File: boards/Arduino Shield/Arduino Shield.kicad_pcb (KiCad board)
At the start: 2 copper layers, 11 parts, among them J1 Screw_Terminal_01x09, J10 Screw_Terminal_01x04, J2 Screw_Terminal_01x09, J3 Screw_Terminal_01x09, J4 Screw_Terminal_01x09, J5 Screw_Terminal_01x09, J6 Screw_Terminal_01x09, J7 Screw_Terminal_01x09, J8 Screw_Terminal_01x09, J9 Screw_Terminal_01x09, U1 A000062

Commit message: Updated pcb
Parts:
- added D1: LED, LED_SMD:LED_0805_2012Metric, F.Cu at (221.0, 99.1)
- added D2: LED, LED_SMD:LED_0805_2012Metric, F.Cu at (219.4, 88.9)
- added D3: LED, LED_SMD:LED_0805_2012Metric, F.Cu at (220.7, 94.0)
- added D4: LED, LED_SMD:LED_0805_2012Metric, F.Cu at (220.7, 109.2)
- added D5: LED, LED_SMD:LED_0805_2012Metric, F.Cu at (221.0, 104.1)
- added J11: Screw_Terminal_01x08, TerminalBlock_4Ucon:TerminalBlock_4Ucon_1x08_P3.50mm_Horizontal, F.Cu at (238.8, 106.2)
- added R1: 6Ω, Resistor_SMD:R_0805_2012Metric, F.Cu at (215.0, 109.2)
- added R2: 6Ω, Resistor_SMD:R_0805_2012Metric, F.Cu at (215.0, 94.0)
- added R3: 6Ω, Resistor_SMD:R_0805_2012Metric, F.Cu at (215.0, 88.9)
- added R4: 230Ω, Resistor_SMD:R_0805_2012Metric, F.Cu at (214.3, 104.1)
- added R5: 6Ω, Resistor_SMD:R_0805_2012Metric, F.Cu at (215.0, 99.1)
- J1: value Screw_Terminal_01x09 -> Screw_Terminal_01x07; footprint TerminalBlock_4Ucon:TerminalBlock_4Ucon_1x09_P3.50mm_Horizontal -> TerminalBlock_4Ucon:TerminalBlock_4Ucon_1x07_P3.50mm_Horizontal
- J10: value Screw_Terminal_01x04 -> Screw_Terminal_01x03; footprint TerminalBlock_4Ucon:TerminalBlock_4Ucon_1x04_P3.50mm_Horizontal -> TerminalBlock_4Ucon:TerminalBlock_4Ucon_1x03_P3.50mm_Horizontal
- J2, J3, J4, J5, J6, J7: value Screw_Terminal_01x09 -> Screw_Terminal_01x08; footprint TerminalBlock_4Ucon:TerminalBlock_4Ucon_1x09_P3.50mm_Horizontal -> TerminalBlock_4Ucon:TerminalBlock_4Ucon_1x08_P3.50mm_Horizontal
- J8: value Screw_Terminal_01x09 -> Screw_Terminal_01x04; footprint TerminalBlock_4Ucon:TerminalBlock_4Ucon_1x09_P3.50mm_Horizontal -> TerminalBlock_4Ucon:TerminalBlock_4Ucon_1x04_P3.50mm_Horizontal
- J9: value Screw_Terminal_01x09 -> Screw_Terminal_01x10; footprint TerminalBlock_4Ucon:TerminalBlock_4Ucon_1x09_P3.50mm_Horizontal -> TerminalBlock_4Ucon:TerminalBlock_4Ucon_1x10_P3.50mm_Horizontal
- moved J4 141.7 mm to (246.3, 75.3), turned to 90 degrees
- moved J5 111.8 mm to (154.9, 38.1), turned to 0 degrees
- moved J1 104.5 mm to (147.3, 121.9), turned to 180 degrees
- moved J3 103.5 mm to (208.3, 121.9), turned to 180 degrees
- moved J9 99.1 mm to (116.8, 38.0)
- moved J6 85.7 mm to (184.7, 38.1), turned to 0 degrees
- moved J8 73.8 mm to (228.6, 85.4), turned to -90 degrees
- moved J2 55.8 mm to (177.8, 121.9), turned to 180 degrees
- moved J10 48.0 mm to (223.5, 70.2)
- moved J7 18.3 mm to (231.2, 39.3)
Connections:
- U1 pad 0: Net-(J3-Pin_9) -> Net-(J5-Pin_8)
- U1 pad 1: Net-(J3-Pin_8) -> Net-(J5-Pin_7)
- U1 pad 10: Net-(J4-Pin_8) -> Net-(J9-Pin_8)
- U1 pad 11: Net-(J4-Pin_7) -> Net-(J9-Pin_7)
- U1 pad 12: Net-(J4-Pin_6) -> Net-(J9-Pin_6)
- U1 pad 13: Net-(J4-Pin_5) -> Net-(J9-Pin_5)
- U1 pad 14: Net-(J8-Pin_1) -> Net-(J6-Pin_1)
- U1 pad 15: Net-(J8-Pin_2) -> Net-(J6-Pin_2)
- U1 pad 16: Net-(J8-Pin_3) -> Net-(J6-Pin_3)
- U1 pad 17: Net-(J8-Pin_4) -> Net-(J6-Pin_4)
- U1 pad 18: Net-(J8-Pin_5) -> Net-(J6-Pin_5)
- U1 pad 19: Net-(J8-Pin_6) -> Net-(J6-Pin_6)
- U1 pad 2: Net-(J3-Pin_7) -> Net-(J5-Pin_6)
- U1 pad 20: Net-(J8-Pin_7) -> Net-(J6-Pin_7)
- U1 pad 21: Net-(J8-Pin_8) -> Net-(J6-Pin_8)
- U1 pad 22: Net-(J1-Pin_7) -> Net-(J4-Pin_7)
- U1 pad 23: Net-(J7-Pin_1) -> Net-(J7-Pin_2)
- U1 pad 24: Net-(J1-Pin_8) -> Net-(J4-Pin_6)
- U1 pad 25: Net-(J7-Pin_2) -> Net-(J7-Pin_3)
- U1 pad 26: Net-(J1-Pin_9) -> Net-(J4-Pin_5)
- U1 pad 27: Net-(J7-Pin_3) -> Net-(J7-Pin_4)
- U1 pad 28: Net-(J5-Pin_1) -> Net-(J4-Pin_4)
- U1 pad 29: Net-(J7-Pin_4) -> Net-(J7-Pin_5)
- U1 pad 3: Net-(J3-Pin_6) -> Net-(J5-Pin_5)
- U1 pad 30: Net-(J5-Pin_2) -> Net-(J4-Pin_3)
- U1 pad 31: Net-(J7-Pin_5) -> Net-(J7-Pin_6)
- U1 pad 32: Net-(J5-Pin_3) -> Net-(J4-Pin_2)
- U1 pad 33: Net-(J7-Pin_6) -> Net-(J7-Pin_7)
- U1 pad 34: Net-(J5-Pin_4) -> Net-(J4-Pin_1)
- U1 pad 35: Net-(J7-Pin_7) -> Net-(J7-Pin_8)
- U1 pad 36: Net-(J5-Pin_5) -> Net-(J11-Pin_8)
- U1 pad 37: Net-(J7-Pin_8) -> Net-(J10-Pin_1)
- U1 pad 38: Net-(J5-Pin_6) -> Net-(J11-Pin_7)
- U1 pad 39: Net-(J7-Pin_9) -> Net-(J10-Pin_2)
- U1 pad 3V3: Net-(J2-Pin_3) -> Net-(J1-Pin_5)
- U1 pad 4: Net-(J3-Pin_5) -> Net-(J5-Pin_4)
- U1 pad 40: Net-(J5-Pin_7) -> Net-(J11-Pin_6)
- U1 pad 41: Net-(J6-Pin_1) -> Net-(J10-Pin_3)
- U1 pad 42: Net-(J5-Pin_8) -> Net-(J11-Pin_5)
- U1 pad 43: Net-(J6-Pin_2) -> Net-(J8-Pin_1)
- U1 pad 44: Net-(J5-Pin_9) -> Net-(J11-Pin_4)
- U1 pad 45: Net-(J6-Pin_3) -> Net-(J8-Pin_2)
- U1 pad 46: Net-(J10-Pin_1) -> Net-(J11-Pin_3)
- U1 pad 47: Net-(J6-Pin_4) -> Net-(J8-Pin_3)
- U1 pad 48: Net-(J10-Pin_2) -> Net-(J11-Pin_2)
- U1 pad 49: Net-(J6-Pin_5) -> Net-(U1-D49)
- U1 pad 5: Net-(J3-Pin_4) -> Net-(J5-Pin_3)
- U1 pad 50: Net-(J10-Pin_3) -> Net-(U1-D50)
- U1 pad 51: Net-(J6-Pin_6) -> Net-(U1-D51)
- U1 pad 52: Net-(J10-Pin_4) -> Net-(U1-D52)
- U1 pad 53: Net-(J6-Pin_7) -> Net-(U1-D53)
- U1 pad 5V_1: Net-(J2-Pin_4) -> Net-(J1-Pin_4)
- U1 pad 5V_2: Net-(J1-Pin_6) -> Net-(J4-Pin_8)
- U1 pad 5V_3: Net-(J8-Pin_9) -> Net-(J7-Pin_1)
- U1 pad 6: Net-(J3-Pin_3) -> Net-(J5-Pin_2)
- U1 pad 7: Net-(J3-Pin_2) -> Net-(J5-Pin_1)
- U1 pad 8: Net-(J3-Pin_1) -> Net-(J9-Pin_10)
- U1 pad 9: Net-(J4-Pin_9) -> Net-(J9-Pin_9)
- U1 pad AD1: Net-(J2-Pin_9) -> Net-(J2-Pin_7)
- U1 pad AD10: Net-(J9-Pin_9) -> Net-(J3-Pin_6)
- U1 pad AD11: Net-(J1-Pin_1) -> Net-(J3-Pin_5)
- U1 pad AD2: Net-(J9-Pin_1) -> Net-(J2-Pin_6)
- U1 pad AD3: Net-(J9-Pin_2) -> Net-(J2-Pin_5)
- U1 pad AD4: Net-(J9-Pin_3) -> Net-(J2-Pin_4)
- U1 pad AD5: Net-(J9-Pin_4) -> Net-(J2-Pin_3)
- U1 pad AD6: Net-(J9-Pin_5) -> Net-(J2-Pin_2)
- U1 pad AD7: Net-(J9-Pin_6) -> Net-(J2-Pin_1)
- U1 pad AD8: Net-(J9-Pin_7) -> Net-(J3-Pin_8)
- U1 pad AD9: Net-(J9-Pin_8) -> Net-(J3-Pin_7)
- U1 pad AREF: Net-(J4-Pin_3) -> Net-(J9-Pin_3)
- U1 pad CANRX0: Net-(J1-Pin_4) -> Net-(J3-Pin_2)
- U1 pad CANTX0: Net-(J1-Pin_5) -> Net-(J3-Pin_1)
- U1 pad DAC0: Net-(J1-Pin_2) -> Net-(J3-Pin_4)
- U1 pad DAC1: Net-(J1-Pin_3) -> Net-(J3-Pin_3)
- U1 pad GND1: Net-(J2-Pin_5) -> Net-(J1-Pin_3)
- U1 pad GND2: Net-(J2-Pin_6) -> Net-(J1-Pin_2)
- U1 pad GND3: Net-(J4-Pin_4) -> Net-(J9-Pin_4)
- U1 pad GND4: Net-(J6-Pin_9) -> Net-(J11-Pin_1)
- U1 pad GND5: Net-(J6-Pin_8) -> Net-(J8-Pin_4)
- U1 pad IOREF: Net-(J2-Pin_1) -> Net-(J1-Pin_7)
- U1 pad RESET: Net-(J2-Pin_2) -> Net-(J1-Pin_6)
- U1 pad SCL: Net-(J4-Pin_1) -> Net-(J9-Pin_1)
- U1 pad SDA: Net-(J4-Pin_2) -> Net-(J9-Pin_2)
- U1 pad VIN: Net-(J2-Pin_7) -> Net-(J1-Pin_1)

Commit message: updated pcb
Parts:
- moved J4 99.8 mm to (147.3, 88.3)
- moved J11 80.8 mm to (160.0, 88.0)
- moved D1 42.3 mm to (185.4, 76.2)
- moved D3 42.3 mm to (185.2, 71.1)
- moved D4 42.3 mm to (185.2, 86.4)
- moved D5 42.3 mm to (185.4, 81.3)
- moved D2 40.2 mm to (186.4, 66.0)
- moved R1 32.3 mm to (192.1, 86.4)
- moved R2 32.3 mm to (192.1, 71.1)
- moved R3 32.3 mm to (192.1, 66.0)
- moved R5 32.3 mm to (192.1, 76.2)
- moved R4 31.8 mm to (192.1, 81.3)
- moved J7 20.0 mm to (213.4, 48.3)
- moved J8 16.4 mm to (213.4, 91.4)
- moved J3 14.5 mm to (201.3, 109.2)
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
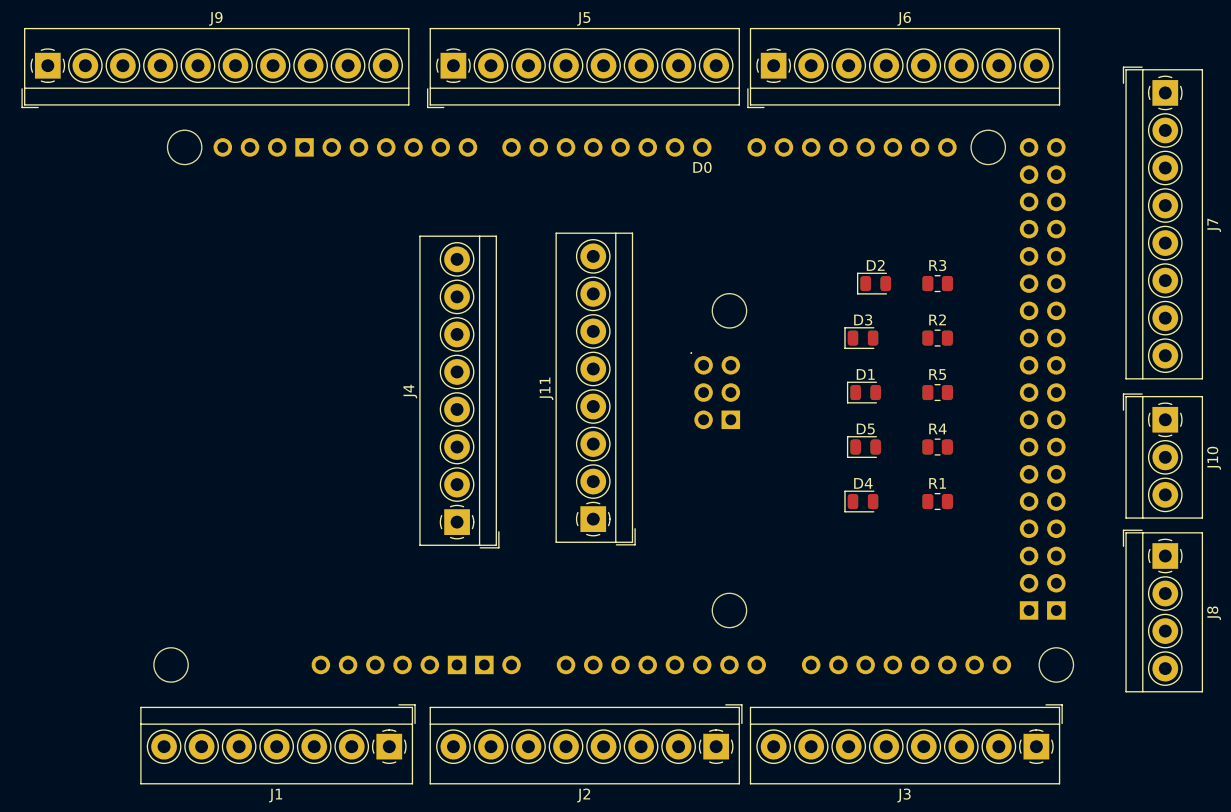
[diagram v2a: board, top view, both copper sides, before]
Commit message: Updated PCB with wiring
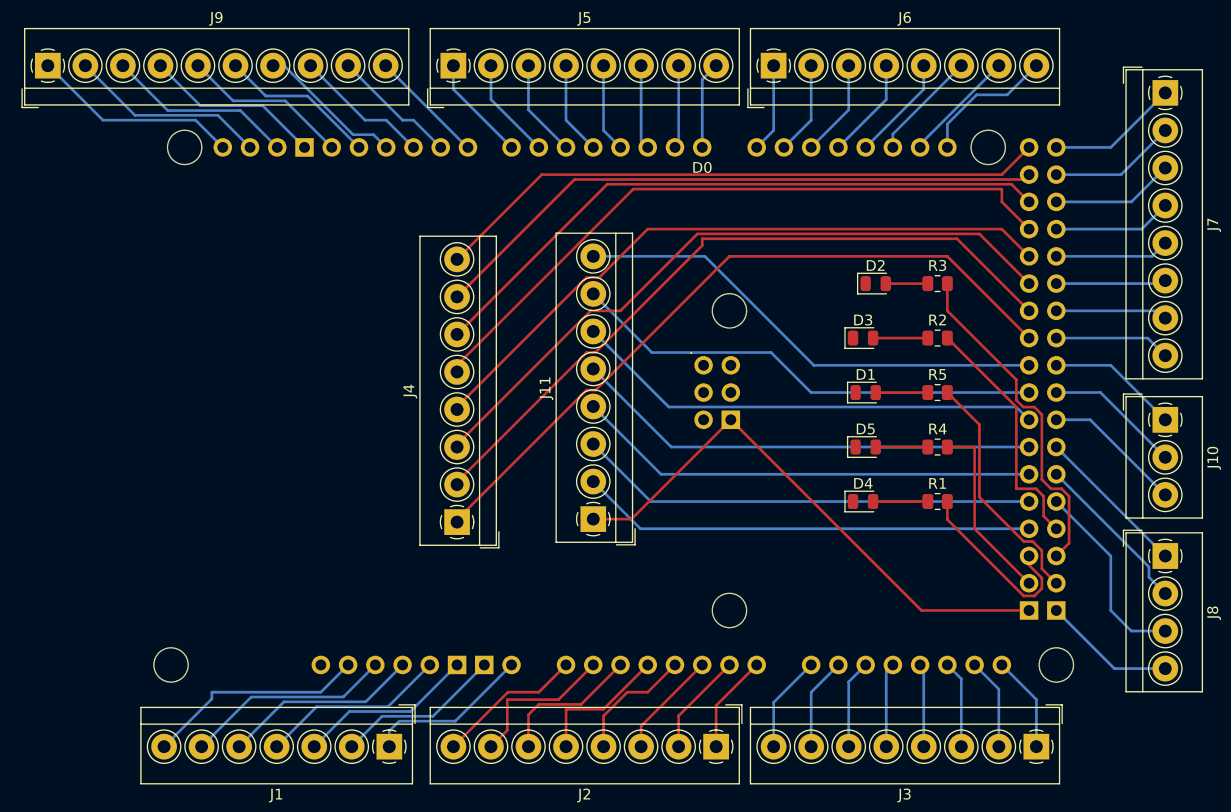
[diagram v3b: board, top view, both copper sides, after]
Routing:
- net Net-(J4-Pin_1): track 0.00 -> 66.9 mm
- net Net-(J4-Pin_2): track 0.00 -> 66.1 mm
- net Net-(J4-Pin_3): track 0.00 -> 63.6 mm
- net Net-(J4-Pin_5): track 0.00 -> 63.0 mm
- net Net-(J4-Pin_4): track 0.00 -> 61.5 mm
- net Net-(J4-Pin_6): track 0.00 -> 59.8 mm
- net Net-(J4-Pin_7): track 0.00 -> 58.1 mm
- net Net-(J4-Pin_8): track 0.00 -> 57.7 mm
- net Net-(J11-Pin_1): track 0.00 -> 51.8 mm
- net Net-(J11-Pin_8): track 0.00 -> 44.8 mm
- net Net-(J11-Pin_7): track 0.00 -> 44.5 mm
- net Net-(J11-Pin_6): track 0.00 -> 44.1 mm
- net Net-(J11-Pin_5): track 0.00 -> 43.7 mm
- net Net-(J11-Pin_4): track 0.00 -> 43.3 mm
- net Net-(J11-Pin_3): track 0.00 -> 42.9 mm
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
